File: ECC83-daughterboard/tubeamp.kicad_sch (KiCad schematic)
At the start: 1 part, among them U2 ECC83

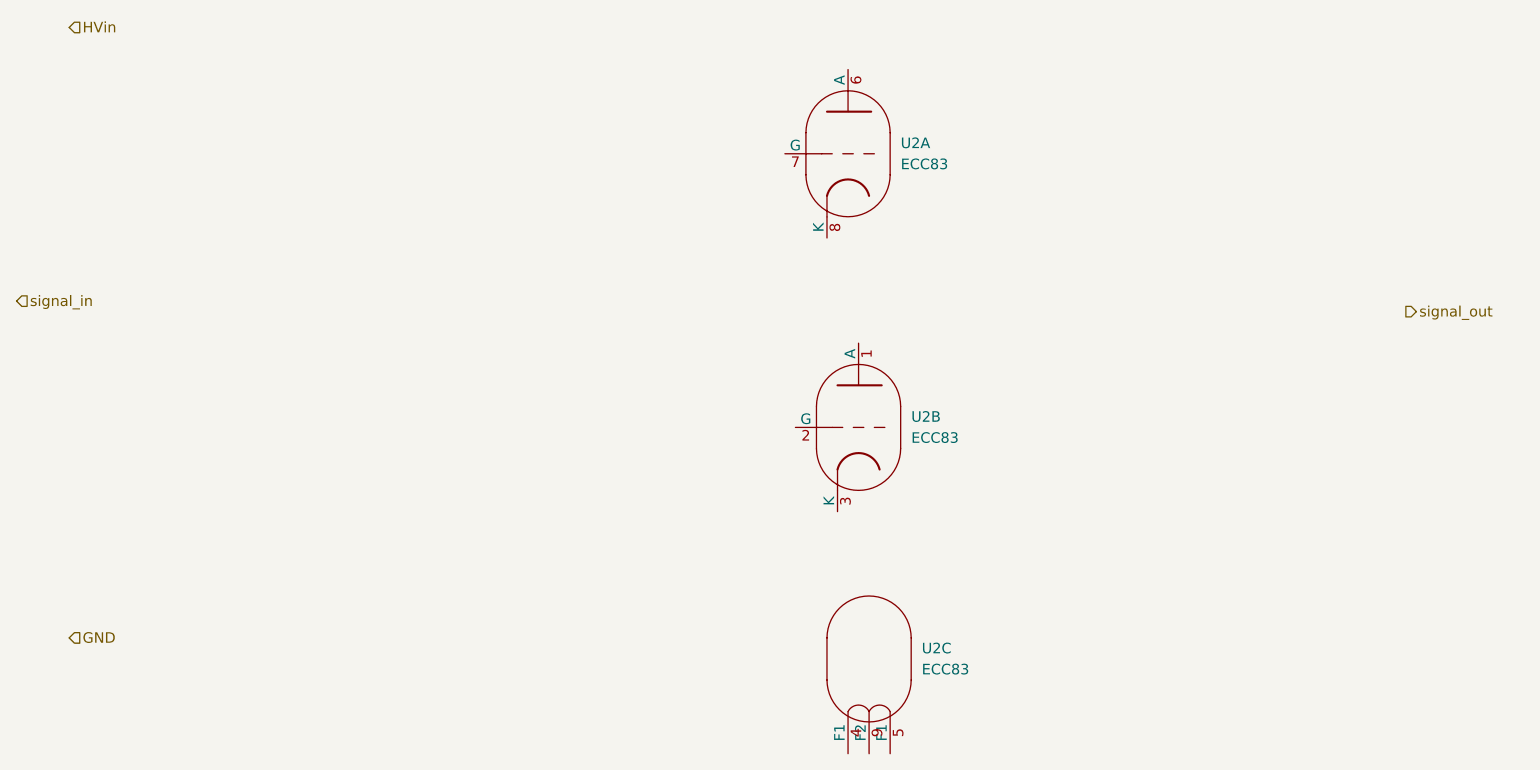
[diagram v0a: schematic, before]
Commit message: HV boost schematic in line with datasheet, half-calculated values
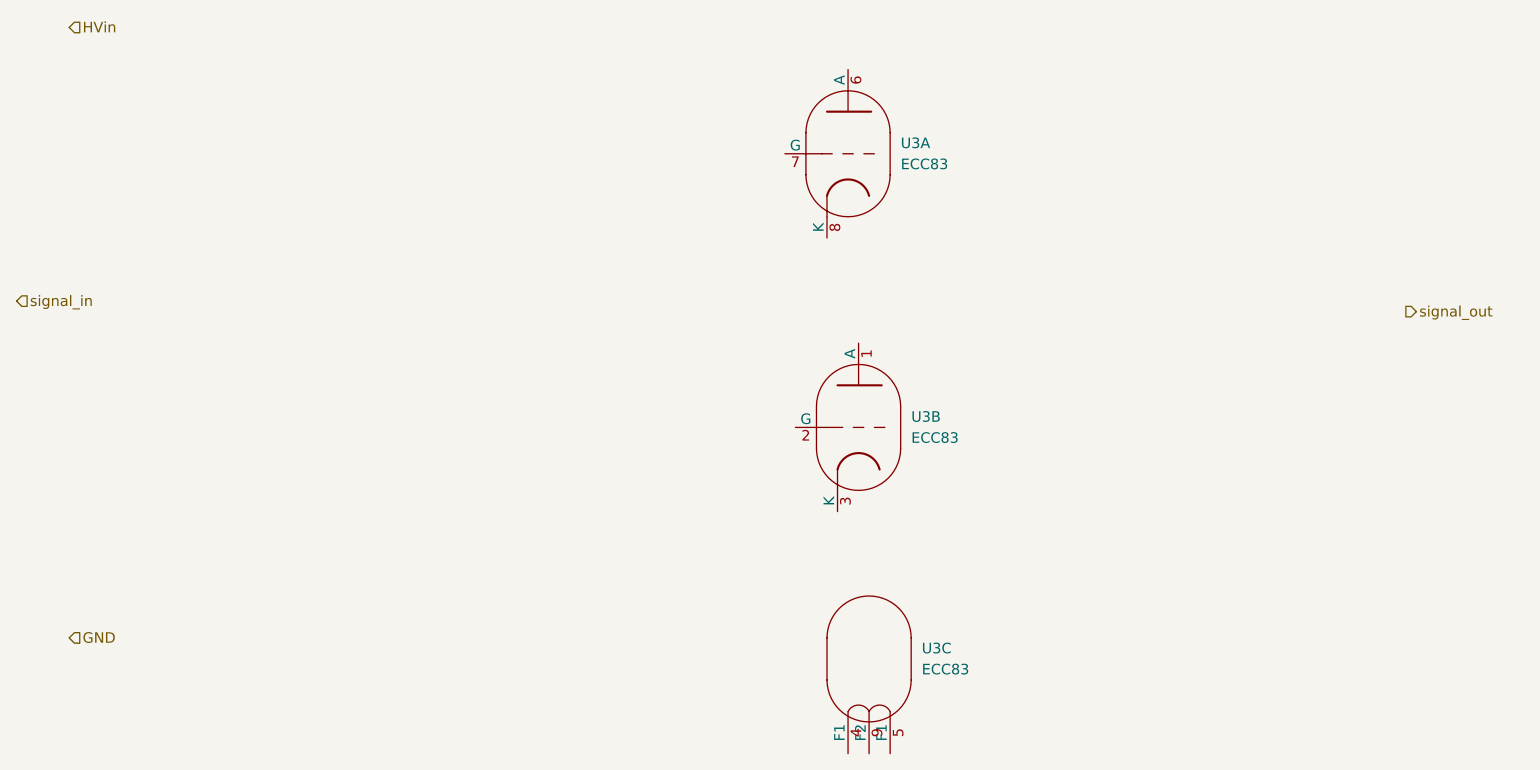
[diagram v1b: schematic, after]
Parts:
- renumbered U2 to U3
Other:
- company: (none) -> nacho.works
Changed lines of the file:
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@@
 	(generator_version "9.0")
 	(paper "A4")
+	(title_block
+		(date "2026-04-20")
+		(company "nacho.works")
+	)
 	(hierarchical_label "GND"
 		(shape input)
@@
 		(dnp no)
 		(fields_autoplaced yes)
-		(property "Reference" "U2"
+		(property "Reference" "U3"
 			(at 156.21 132.0799 0)
 			(effects
@@
 			(project "ECC83-daughterboard"
 				(path "/6631e6c4-daf1-4ebd-bf40-608d44fc040a/f8ad7e96-0a45-4b98-93c8-0be9b35d34fa"
-					(reference "U2")
+					(reference "U3")
 					(unit 3)
 				)
@@
 		(dnp no)
 		(fields_autoplaced yes)
-		(property "Reference" "U2"
+		(property "Reference" "U3"
 			(at 153.67 71.1199 0)
 			(effects
@@
 			(project "ECC83-daughterboard"
 				(path "/6631e6c4-daf1-4ebd-bf40-608d44fc040a/f8ad7e96-0a45-4b98-93c8-0be9b35d34fa"
-					(reference "U2")
+					(reference "U3")
 					(unit 1)
 				)
@@
 		(dnp no)
 		(fields_autoplaced yes)
-		(property "Reference" "U2"
+		(property "Reference" "U3"
 			(at 154.94 104.1399 0)
 			(effects
@@
 			(project "ECC83-daughterboard"
 				(path "/6631e6c4-daf1-4ebd-bf40-608d44fc040a/f8ad7e96-0a45-4b98-93c8-0be9b35d34fa"
-					(reference "U2")
+					(reference "U3")
 					(unit 2)
 				)
